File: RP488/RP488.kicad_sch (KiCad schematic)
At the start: 25 parts, among them J1 GPIB, J2 Test, U1 SN75160, U2 SN75161, U3 SN74LV245ATDW

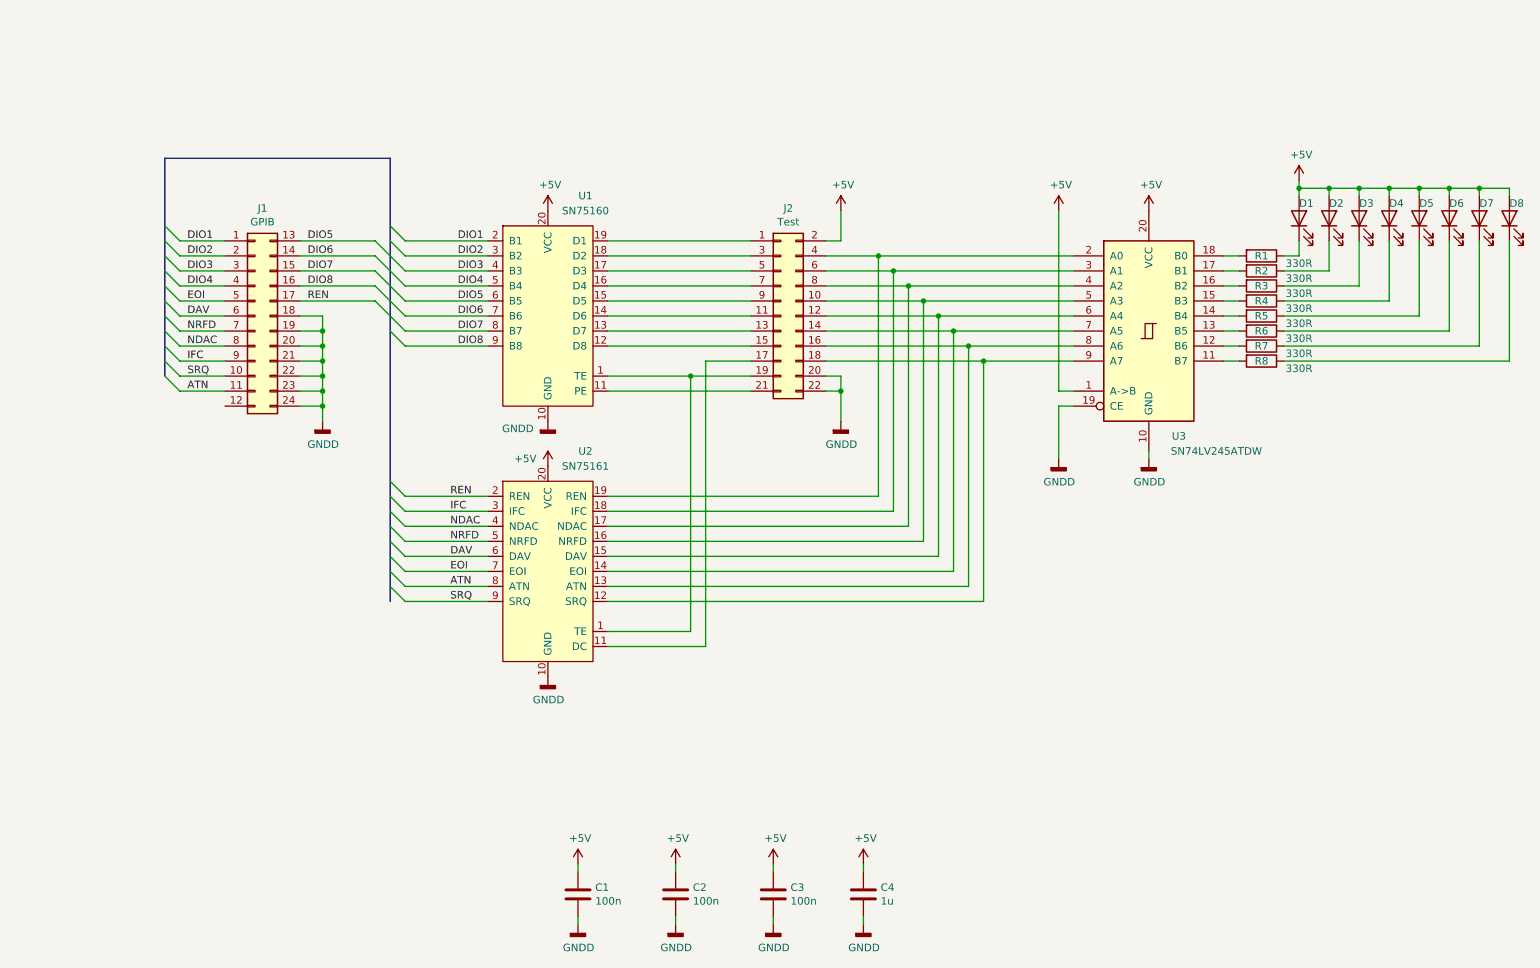
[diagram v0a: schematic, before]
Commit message: Changed design to RP2354
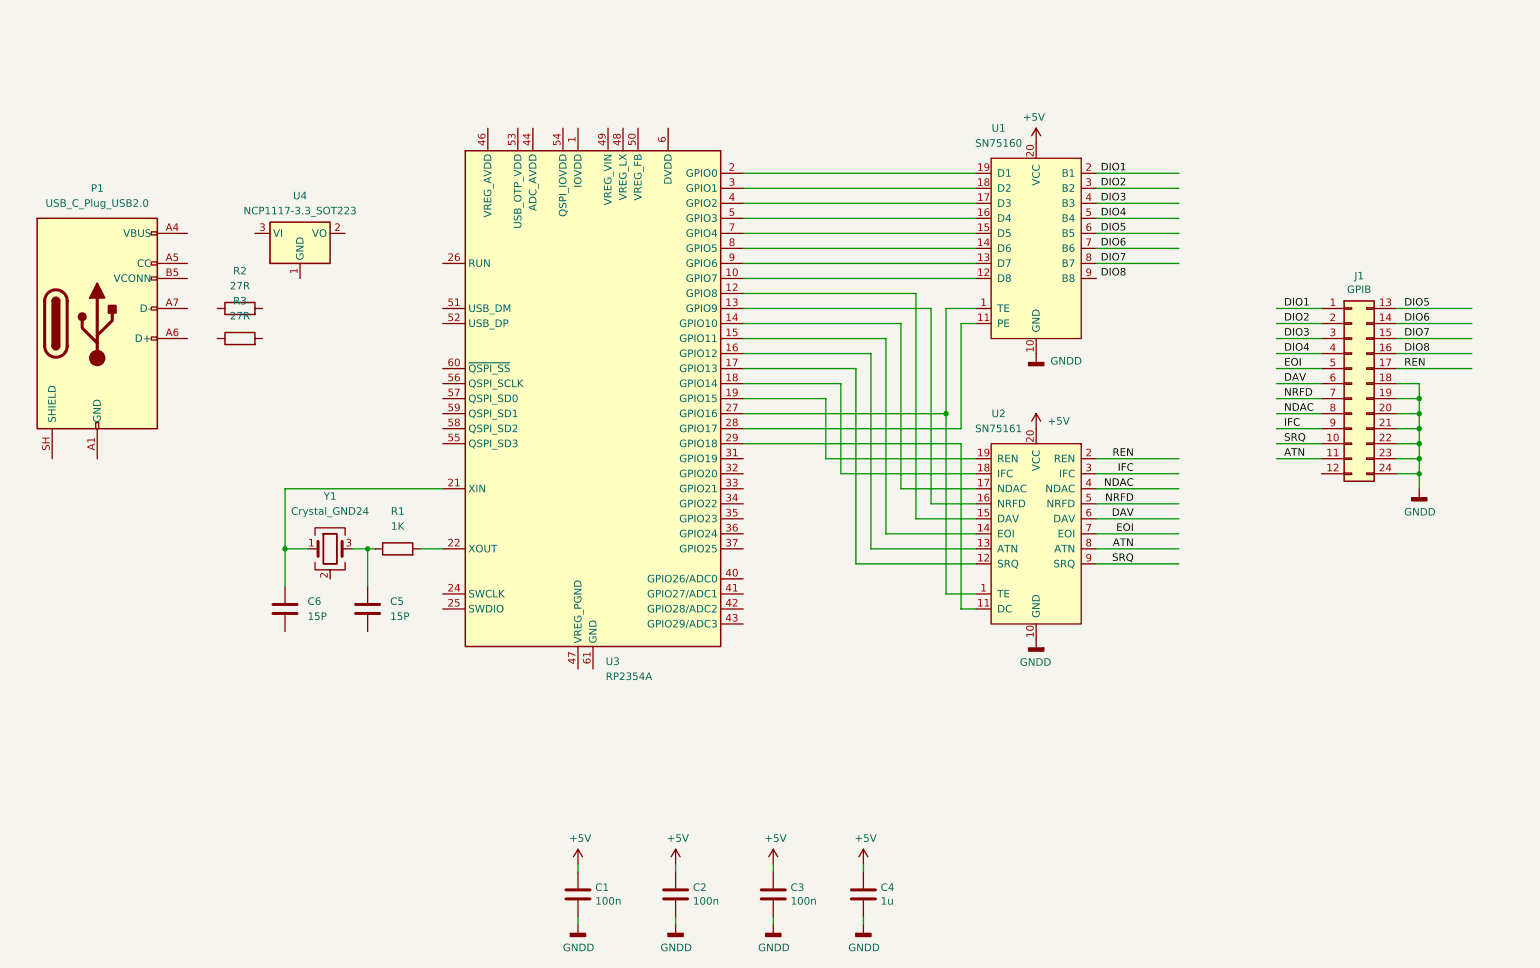
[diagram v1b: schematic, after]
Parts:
- removed D1, D2, D3, D4, D5, D6, D7, D8: LED, LED_SMD:LED_0805_2012Metric, symbol Device:LED
- removed J2: Test, Connector_PinHeader_2.54mm:PinHeader_2x11_P2.54mm_Vertical, symbol Connector_Generic:Conn_02x11_Odd_Even
- removed R4, R5, R6, R7, R8: 330R, Resistor_SMD:R_0603_1608Metric, symbol Device:R
- removed U3: SN74LV245ATDW, Package_SO:SO-20_12.8x7.5mm_P1.27mm, symbol 74xx:74HC245
- added C5, C6: 15P, symbol Device:C
- added P1: USB_C_Plug_USB2.0, Package_DFN_QFN:QFN-60-1EP_7x7mm_P0.4mm_EP3.4x3.4mm, symbol Connector:USB_C_Plug_USB2.0
- added U3: RP2354A, Package_DFN_QFN:QFN-60-1EP_7x7mm_P0.4mm_EP3.4x3.4mm, symbol MCU_RaspberryPi:RP2354A
- added U4: NCP1117-3.3_SOT223, Package_TO_SOT_SMD:SOT-223-3_TabPin2, symbol Regulator_Linear:NCP1117-3.3_SOT223
- added Y1: Crystal_GND24, Package_TO_SOT_SMD:SOT-223-3_TabPin2, symbol Device:Crystal_GND24
- R1: value 330R -> 1K; footprint Resistor_SMD:R_0603_1608Metric -> (none)
- R2, R3: value 330R -> 27R; footprint Resistor_SMD:R_0603_1608Metric -> (none)
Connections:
- net DIO8: no longer U1.9 (B8)
- net at U1.1 (TE), U2.1 (TE): now also U3.27 (GPIO16)
- net at U1.11 (PE): now also U3.28 (GPIO17)
- net at U1.12 (D8): now also U3.10 (GPIO7)
- net at U1.13 (D7): now also U3.9 (GPIO6)
- net at U1.14 (D6): now also U3.8 (GPIO5)
- net at U1.15 (D5): now also U3.7 (GPIO4)
- net at U1.16 (D4): now also U3.5 (GPIO3)
- net at U1.17 (D3): now also U3.4 (GPIO2)
- net at U1.18 (D2): now also U3.3 (GPIO1)
- net at U1.19 (D1): now also U3.2 (GPIO0)
- net at U2.11 (DC): now also U3.29 (GPIO18)
- net at U2.12 (SRQ): now also U3.17 (GPIO13)
- net at U2.13 (ATN): now also U3.16 (GPIO12)
- net at U2.14 (EOI): now also U3.15 (GPIO11)
- net at U2.15 (DAV): now also U3.12 (GPIO8)
- net at U2.16 (NRFD): now also U3.13 (GPIO9)
- net at U2.17 (NDAC): now also U3.14 (GPIO10)
- net at U2.18 (IFC): now also U3.18 (GPIO14)
- net at U2.19 (REN): now also U3.19 (GPIO15)
- net at R1.2: now also U3.22 (XOUT)
- net at R1.1: now also C5.1, Y1.3
- new net: U3.1 (IOVDD), U3.11 (IOVDD), U3.20 (IOVDD), U3.30 (IOVDD), U3.38 (IOVDD), U3.45 (IOVDD)
- new net: C6.1, U3.21 (XIN), Y1.1
- new net: U3.23 (DVDD), U3.39 (DVDD), U3.6 (DVDD)
- new net: P1.A1 (GND), P1.A12 (GND), P1.B1 (GND), P1.B12 (GND)
- new net: P1.A4 (VBUS), P1.A9 (VBUS), P1.B4 (VBUS), P1.B9 (VBUS)
- new net: Y1.2 (G), Y1.4 (G)
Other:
- moved on the sheet: J1, U1, U2

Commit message: SWD connector and schematic changes
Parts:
- removed P1: USB_C_Plug_USB2.0, Package_DFN_QFN:QFN-60-1EP_7x7mm_P0.4mm_EP3.4x3.4mm, symbol Connector:USB_C_Plug_USB2.0
- removed U4: NCP1117-3.3_SOT223, Package_TO_SOT_SMD:SOT-223-3_TabPin2, symbol Regulator_Linear:NCP1117-3.3_SOT223
- removed Y1: Crystal_GND24, Package_TO_SOT_SMD:SOT-223-3_TabPin2, symbol Device:Crystal_GND24
- added C10, C11, C9: 100n, Capacitor_SMD:C_0603_1608Metric, symbol Device:C
- added C12, C13: 100n, symbol Device:C
- added C7, C8: 4U7, symbol Device:C
- added D1, D2: LED, LED_SMD:LED_1206_3216Metric, symbol Device:LED
- added J2: SWD, GPIB:PinHeader_2x05_P1.27mm_Vertical_SMD, symbol USB:Conn_02x05_Odd_Even
- added J3: USB Mini, GPIB:USB_Mini_B_Female_690-005-299-043, symbol USB:690-005-299-043-dk_USB-DVI-HDMI-Connectors
- added L1: L, symbol Device:L
- added R4: 33R, Resistor_SMD:R_0603_1608Metric, symbol Device:R
- added R5, R6: 1K, Resistor_SMD:R_0603_1608Metric, symbol Device:R
- added U5: USBLC6-2SC6, Package_TO_SOT_SMD:SOT-23-6, symbol USB:USBLC6-2SC6-Power_Protection
- added U6: LD3985M33R_SOT23, Package_TO_SOT_SMD:SOT-23-5, symbol USB:LD3985M33R_SOT23
- added XTAL1: 12MHz, GPIB:SMD-2_3.2x1.5mm, symbol USB:ECS-_327-12_5-34B-TR-dk_Crystals
- R2, R3: footprint (none) -> Resistor_SMD:R_0603_1608Metric
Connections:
- net +5V: now also C13.1, J3.1, U5.5 (VBUS), U6.1 (VIN), U6.3 (INH)
- net GNDD: now also C5.2, C6.2, U3.47 (VREG_PGND), U3.61 (GND), C10.2, C11.2, C12.2, C13.2, C7.2, C8.2, C9.2, J2.3 (Pin_3), J2.5 (Pin_5), J3.5, J3.SH, R5.2, R6.2, U5.2 (GND), U6.2 (GND)
- net at R3.1: now also U5.6 (IO1)
- net at R3.2: now also U3.51 (USB_DM)
- net +3V3: now reaches U3.1 (IOVDD), U3.11 (IOVDD), U3.20 (IOVDD), U3.30 (IOVDD), U3.38 (IOVDD), U3.45 (IOVDD)
- net +3V3: now also U3.26 (RUN), U3.44 (ADC_AVDD), U3.49 (VREG_VIN), U3.53 (USB_OTP_VDD), U3.54 (QSPI_IOVDD), C10.1, C11.1, C9.1, J2.1 (Pin_1), R4.2, U6.5 (VOUT)
- net at C6.1, U3.21 (XIN): now also XTAL1.1
- net at U3.23 (DVDD), U3.39 (DVDD), U3.6 (DVDD): now also U3.50 (VREG_FB), C8.1, L1.1
- net SWDCLK: now reaches U3.24 (SWCLK)
- net SWDCLK: now also J2.4 (Pin_4)
- net SWDIO: now reaches U3.25 (SWDIO)
- net SWDIO: now also J2.2 (Pin_2)
- net at U3.31 (GPIO19): now also D1.2 (A)
- net at U3.32 (GPIO20): now also D2.2 (A)
- net at U3.46 (VREG_AVDD): now also C7.1, R4.1
- net at U3.48 (VREG_LX): now also L1.2
- net at U3.52 (USB_DP): now also R2.2
- net at C5.1, R1.1: now also XTAL1.2
- net at R2.1: now also U5.4 (IO2)
- new net: D1.1 (K), R5.1
- new net: C12.1, U6.4 (BYP)
- new net: J3.2, U5.1 (IO1)
- new net: J3.3, U5.3 (IO2)
- new net: D2.1 (K), R6.1
- new net SWO: J2.6 (Pin_6)
- new net TDI: J2.8 (Pin_8)
- new net nRESET: J2.10 (Pin_10)
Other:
- moved on the sheet: R2, R3

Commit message: Switch to RP2354
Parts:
- added C14, C15: 100n, Capacitor_SMD:C_0603_1608Metric, symbol Device:C
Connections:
- net +3V3: now also C14.1, C15.1
- net DIO8: now also U1.9 (B8)
- net GNDD: now also C14.2, C15.2
